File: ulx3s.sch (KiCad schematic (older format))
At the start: 2 parts, among them U1 LFE5U-25F-6BG381C

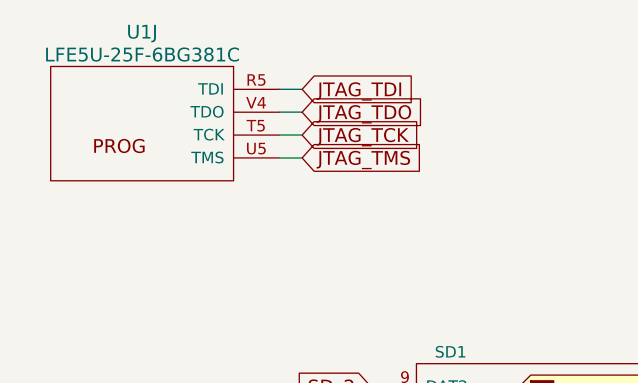
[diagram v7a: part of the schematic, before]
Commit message: JTAG port to USB sheet
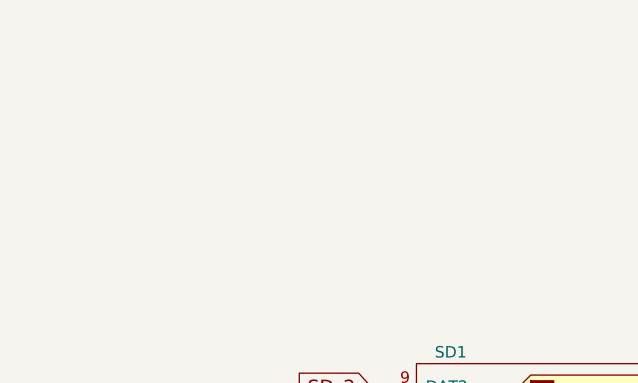
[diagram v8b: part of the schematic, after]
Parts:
- removed U1: LFE5U-25F-6BG381C, lfe5bg381:BGA-381_pitch0.8mm_dia0.4mm, symbol LFE5-BG381
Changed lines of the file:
@@
 Comment4 ""
 $EndDescr
-Wire Wire Line
-	2000 4650 1900 4650
-Wire Wire Line
-	2000 4550 1900 4550
-Wire Wire Line
-	1900 4850 2000 4850
 $Comp
 L SD_Card SD1
@@
 	1    3300 6250
 	1    0    0    -1
-$EndComp
-$Comp
-L LFE5-BG381 U1
-U 10 1 56AAA6F3
-P 1200 4700
-F 0 "U1" H 1100 5100 60  0000 C CNN
-F 1 "LFE5U-25F-6BG381C" H 1100 5000 60  0000 C CNN
-F 2 "lfe5bg381:BGA-381_pitch0.8mm_dia0.4mm" H 150 5650 60  0001 C CNN
-F 3 "" H 150 5650 60  0000 C CNN
-	10   1200 4700
-	-1   0    0    -1
 $EndComp
 Wire Wire Line
@@
 	1850 6450 2400 6450
 $Comp
-L GND #PWR01
+L GND #PWR2
 U 1 1 58D58197
 P 1850 6150
-F 0 "#PWR01" H 1850 5900 50  0001 C CNN
+F 0 "#PWR2" H 1850 5900 50  0001 C CNN
 F 1 "GND" H 1850 6000 50  0000 C CNN
 F 2 "" H 1850 6150 50  0000 C CNN
@@
 $EndComp
 $Comp
-L GND #PWR02
+L GND #PWR3
 U 1 1 58D581BF
 P 1850 6450
-F 0 "#PWR02" H 1850 6200 50  0001 C CNN
+F 0 "#PWR3" H 1850 6200 50  0001 C CNN
 F 1 "GND" H 1850 6300 50  0000 C CNN
 F 2 "" H 1850 6450 50  0000 C CNN
@@
 SD_WP
 $Comp
-L GND #PWR03
+L GND #PWR4
 U 1 1 58D58733
 P 4300 6550
-F 0 "#PWR03" H 4300 6300 50  0001 C CNN
+F 0 "#PWR4" H 4300 6300 50  0001 C CNN
 F 1 "GND" H 4300 6400 50  0000 C CNN
 F 2 "" H 4300 6550 50  0000 C CNN
@@
 Connection ~ 4300 6450
 $Comp
-L +3V3 #PWR04
+L +3V3 #PWR1
 U 1 1 58D5F123
 P 1700 6250
-F 0 "#PWR04" H 1700 6100 50  0001 C CNN
+F 0 "#PWR1" H 1700 6100 50  0001 C CNN
 F 1 "+3V3" H 1700 6390 50  0000 C CNN
 F 2 "" H 1700 6250 50  0000 C CNN
@@
 F1 "ram.sch" 60
 $EndSheet
-Text GLabel 2000 4550 2    60   Input ~ 0
-JTAG_TDI
-Text GLabel 2000 4650 2    60   Input ~ 0
-JTAG_TDO
-Text GLabel 2000 4750 2    60   Input ~ 0
-JTAG_TCK
-Text GLabel 2000 4850 2    60   Input ~ 0
-JTAG_TMS
-Wire Wire Line
-	1900 4750 2000 4750
 Text GLabel 2300 5850 0    60   Input ~ 0
 SD_2
